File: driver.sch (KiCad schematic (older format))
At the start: 45 parts, among them J1 Screw_Terminal_01x02, J2 Conn_02x12_Odd_Even, Q10 Q_NMOS_GDSD, Q11 Q_NMOS_GDSD, Q12 Q_NMOS_GDSD, Q13 Q_NMOS_GDSD, Q14 Q_NMOS_GDSD, Q15 Q_NMOS_GDSD, Q16 Q_NMOS_GDSD, Q17 IRF9Z34 PMOS_DGS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

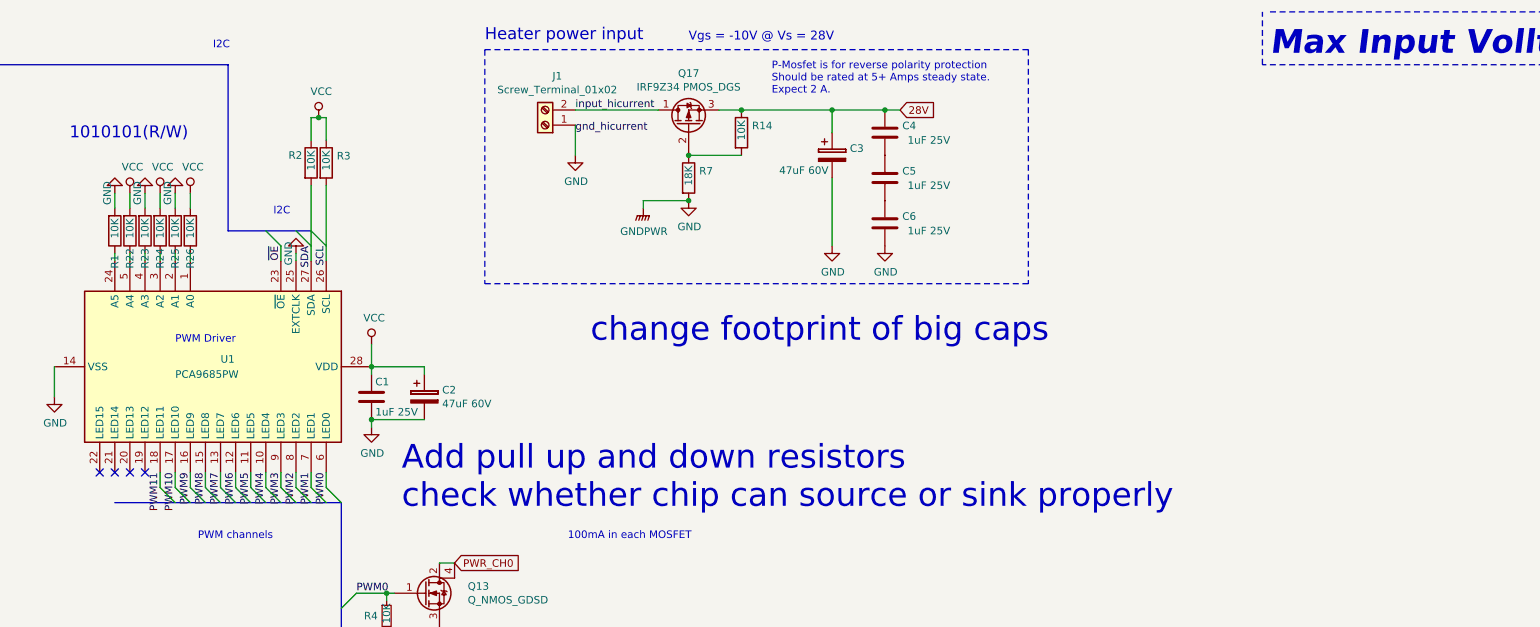
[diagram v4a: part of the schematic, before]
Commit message: resistor value/footprint changes and associated routing changes
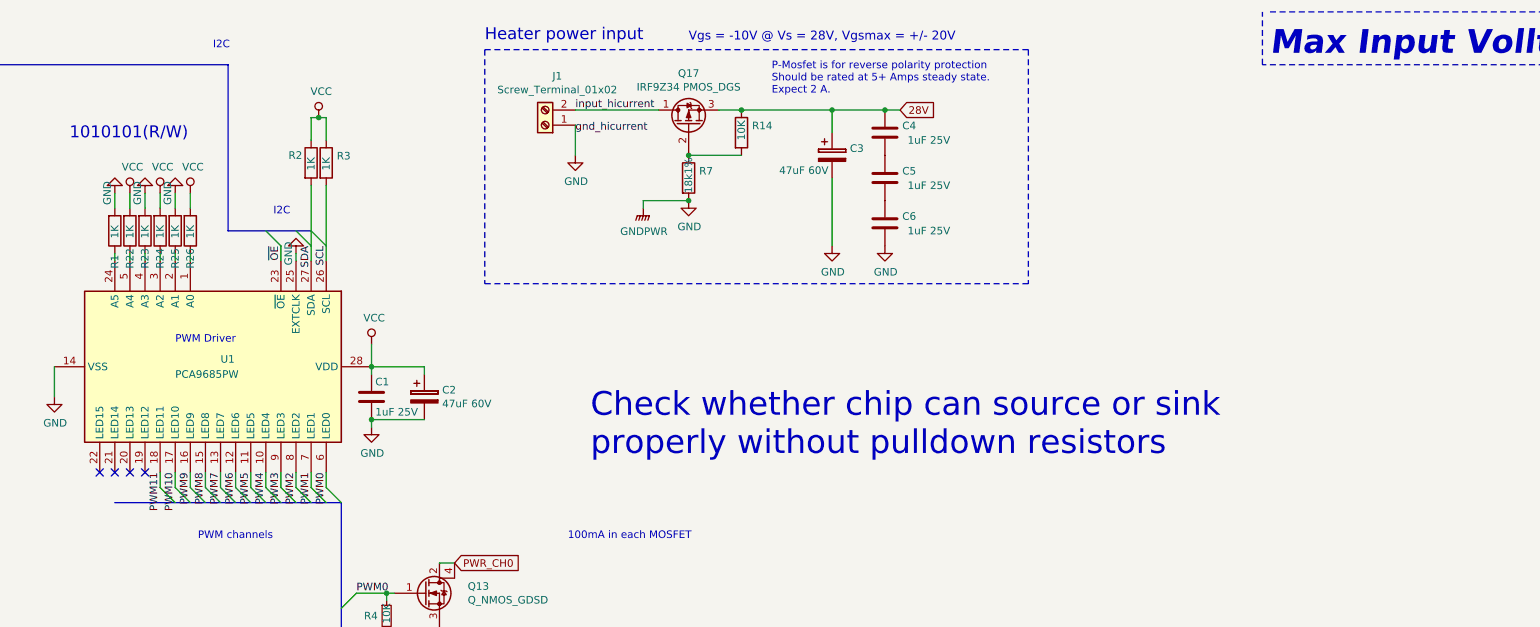
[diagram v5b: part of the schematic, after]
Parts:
- R1, R2, R22, R23, R24, R25, R26, R3: value 10K -> 1K
- R10, R11, R12, R13, R14, R18, R19, R20, R21, R4, R5, R6, R9: footprint Resistor_SMD:R_0805_2012Metric_Pad1.15x1.40mm_HandSolder -> Resistor_SMD:R_1206_3216Metric_Pad1.42x1.75mm_HandSolder
- R7: value 18K -> 18k1%; footprint Resistor_SMD:R_0805_2012Metric_Pad1.15x1.40mm_HandSolder -> Resistor_SMD:R_1206_3216Metric_Pad1.42x1.75mm_HandSolder
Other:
- note added: "Check whether chip can source or sink \nproperly without pulldown resistors"
- note added: "Vgs = -10V @ Vs = 28V, Vgsmax = +/- 20V"
- note removed: "Add pull up and down resistors\ncheck whether chip can source or sink properly"
- note removed: "Vgs = -10V @ Vs = 28V"
- note removed: "change footprint of big caps"
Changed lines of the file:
@@
 P 5100 2150
 F 0 "R1" V 5100 2400 50  0000 R CNN
-F 1 "10K" V 5100 2200 50  0000 R CNN
+F 1 "1K" V 5100 2200 50  0000 R CNN
 F 2 "Resistor_SMD:R_0805_2012Metric_Pad1.15x1.40mm_HandSolder" V 5030 2150 50  0001 C CNN
 F 3 "~" H 5100 2150 50  0001 C CNN
@@
 P 8900 1800
 F 0 "R7" H 8970 1846 50  0000 L CNN
-F 1 "18K" V 8900 1750 50  0000 L CNN
-F 2 "Resistor_SMD:R_0805_2012Metric_Pad1.15x1.40mm_HandSolder" V 8830 1800 50  0001 C CNN
+F 1 "18k1%" V 8900 1700 50  0000 L CNN
+F 2 "Resistor_SMD:R_1206_3216Metric_Pad1.42x1.75mm_HandSolder" V 8830 1800 50  0001 C CNN
 F 3 "~" H 8900 1800 50  0001 C CNN
 	1    8900 1800
@@
 P 6500 1700
 F 0 "R3" H 6570 1746 50  0000 L CNN
-F 1 "10K" V 6500 1650 50  0000 L CNN
+F 1 "1K" V 6500 1650 50  0000 L CNN
 F 2 "Resistor_SMD:R_0805_2012Metric_Pad1.15x1.40mm_HandSolder" V 6430 1700 50  0001 C CNN
 F 3 "~" H 6500 1700 50  0001 C CNN
@@
 P 6400 1700
 F 0 "R2" H 6250 1750 50  0000 L CNN
-F 1 "10K" V 6400 1650 50  0000 L CNN
+F 1 "1K" V 6400 1650 50  0000 L CNN
 F 2 "Resistor_SMD:R_0805_2012Metric_Pad1.15x1.40mm_HandSolder" V 6330 1700 50  0001 C CNN
 F 3 "~" H 6400 1700 50  0001 C CNN
@@
 	6500 1400 6500 1550
 Connection ~ 6450 1400
-Text Notes 7000 4000 0    157  ~ 0
-Add pull up and down resistors\ncheck whether chip can source or sink properly
-Text Notes 8250 2900 0    157  ~ 0
-change footprint of big caps
+Text Notes 8250 3650 0    157  ~ 0
+Check whether chip can source or sink \nproperly without pulldown resistors
 $Comp
 L Device:R_Small R4
@@
 F 0 "R4" H 6750 4700 50  0000 L CNN
 F 1 "10K" V 6900 4650 50  0000 L CNN
-F 2 "Resistor_SMD:R_0805_2012Metric_Pad1.15x1.40mm_HandSolder" H 6900 4700 50  0001 C CNN
+F 2 "Resistor_SMD:R_1206_3216Metric_Pad1.42x1.75mm_HandSolder" H 6900 4700 50  0001 C CNN
 F 3 "~" H 6900 4700 50  0001 C CNN
 	1    6900 4700
@@
 F 0 "R5" H 6750 5300 50  0000 L CNN
 F 1 "10K" V 6900 5250 50  0000 L CNN
-F 2 "Resistor_SMD:R_0805_2012Metric_Pad1.15x1.40mm_HandSolder" H 6900 5300 50  0001 C CNN
+F 2 "Resistor_SMD:R_1206_3216Metric_Pad1.42x1.75mm_HandSolder" H 6900 5300 50  0001 C CNN
 F 3 "~" H 6900 5300 50  0001 C CNN
 	1    6900 5300
@@
 F 0 "R6" H 6750 5900 50  0000 L CNN
 F 1 "10K" V 6900 5850 50  0000 L CNN
-F 2 "Resistor_SMD:R_0805_2012Metric_Pad1.15x1.40mm_HandSolder" H 6900 5900 50  0001 C CNN
+F 2 "Resistor_SMD:R_1206_3216Metric_Pad1.42x1.75mm_HandSolder" H 6900 5900 50  0001 C CNN
 F 3 "~" H 6900 5900 50  0001 C CNN
 	1    6900 5900
@@
 F 0 "R9" H 6750 6500 50  0000 L CNN
 F 1 "10K" V 6900 6450 50  0000 L CNN
-F 2 "Resistor_SMD:R_0805_2012Metric_Pad1.15x1.40mm_HandSolder" H 6900 6500 50  0001 C CNN
+F 2 "Resistor_SMD:R_1206_3216Metric_Pad1.42x1.75mm_HandSolder" H 6900 6500 50  0001 C CNN
 F 3 "~" H 6900 6500 50  0001 C CNN
 	1    6900 6500
@@
 F 0 "R10" H 6700 7100 50  0000 L CNN
 F 1 "10K" V 6900 7050 50  0000 L CNN
-F 2 "Resistor_SMD:R_0805_2012Metric_Pad1.15x1.40mm_HandSolder" H 6900 7100 50  0001 C CNN
+F 2 "Resistor_SMD:R_1206_3216Metric_Pad1.42x1.75mm_HandSolder" H 6900 7100 50  0001 C CNN
 F 3 "~" H 6900 7100 50  0001 C CNN
 	1    6900 7100
@@
 F 0 "R11" H 6700 7700 50  0000 L CNN
 F 1 "10K" V 6900 7650 50  0000 L CNN
-F 2 "Resistor_SMD:R_0805_2012Metric_Pad1.15x1.40mm_HandSolder" H 6900 7700 50  0001 C CNN
+F 2 "Resistor_SMD:R_1206_3216Metric_Pad1.42x1.75mm_HandSolder" H 6900 7700 50  0001 C CNN
 F 3 "~" H 6900 7700 50  0001 C CNN
 	1    6900 7700
@@
 F 0 "R12" H 6700 8300 50  0000 L CNN
 F 1 "10K" V 6900 8250 50  0000 L CNN
-F 2 "Resistor_SMD:R_0805_2012Metric_Pad1.15x1.40mm_HandSolder" H 6900 8300 50  0001 C CNN
+F 2 "Resistor_SMD:R_1206_3216Metric_Pad1.42x1.75mm_HandSolder" H 6900 8300 50  0001 C CNN
 F 3 "~" H 6900 8300 50  0001 C CNN
 	1    6900 8300
@@
 F 0 "R13" H 6700 8900 50  0000 L CNN
 F 1 "10K" V 6900 8850 50  0000 L CNN
-F 2 "Resistor_SMD:R_0805_2012Metric_Pad1.15x1.40mm_HandSolder" H 6900 8900 50  0001 C CNN
+F 2 "Resistor_SMD:R_1206_3216Metric_Pad1.42x1.75mm_HandSolder" H 6900 8900 50  0001 C CNN
 F 3 "~" H 6900 8900 50  0001 C CNN
 	1    6900 8900
@@
 F 0 "R21" H 8150 8900 50  0000 L CNN
 F 1 "10K" V 8350 8850 50  0000 L CNN
-F 2 "Resistor_SMD:R_0805_2012Metric_Pad1.15x1.40mm_HandSolder" H 8350 8900 50  0001 C CNN
+F 2 "Resistor_SMD:R_1206_3216Metric_Pad1.42x1.75mm_HandSolder" H 8350 8900 50  0001 C CNN
 F 3 "~" H 8350 8900 50  0001 C CNN
 	1    8350 8900
@@
 F 0 "R20" H 8100 8300 50  0000 L CNN
 F 1 "10K" V 8300 8250 50  0000 L CNN
-F 2 "Resistor_SMD:R_0805_2012Metric_Pad1.15x1.40mm_HandSolder" H 8300 8300 50  0001 C CNN
+F 2 "Resistor_SMD:R_1206_3216Metric_Pad1.42x1.75mm_HandSolder" H 8300 8300 50  0001 C CNN
 F 3 "~" H 8300 8300 50  0001 C CNN
 	1    8300 8300
@@
 F 0 "R19" H 8100 7700 50  0000 L CNN
 F 1 "10K" V 8300 7650 50  0000 L CNN
-F 2 "Resistor_SMD:R_0805_2012Metric_Pad1.15x1.40mm_HandSolder" H 8300 7700 50  0001 C CNN
+F 2 "Resistor_SMD:R_1206_3216Metric_Pad1.42x1.75mm_HandSolder" H 8300 7700 50  0001 C CNN
 F 3 "~" H 8300 7700 50  0001 C CNN
 	1    8300 7700
@@
 F 0 "R18" H 8100 7100 50  0000 L CNN
 F 1 "10K" V 8300 7050 50  0000 L CNN
-F 2 "Resistor_SMD:R_0805_2012Metric_Pad1.15x1.40mm_HandSolder" H 8300 7100 50  0001 C CNN
+F 2 "Resistor_SMD:R_1206_3216Metric_Pad1.42x1.75mm_HandSolder" H 8300 7100 50  0001 C CNN
 F 3 "~" H 8300 7100 50  0001 C CNN
 	1    8300 7100
@@
 P 5300 2150
 F 0 "R23" V 5300 2400 50  0000 R CNN
-F 1 "10K" V 5300 2200 50  0000 R CNN
+F 1 "1K" V 5300 2200 50  0000 R CNN
 F 2 "Resistor_SMD:R_0805_2012Metric_Pad1.15x1.40mm_HandSolder" V 5230 2150 50  0001 C CNN
 F 3 "~" H 5300 2150 50  0001 C CNN
@@
 P 5400 2150
 F 0 "R24" V 5400 2400 50  0000 R CNN
-F 1 "10K" V 5400 2200 50  0000 R CNN
+F 1 "1K" V 5400 2200 50  0000 R CNN
 F 2 "Resistor_SMD:R_0805_2012Metric_Pad1.15x1.40mm_HandSolder" V 5330 2150 50  0001 C CNN
 F 3 "~" H 5400 2150 50  0001 C CNN
@@
 P 5200 2150
 F 0 "R22" V 5200 2400 50  0000 R CNN
-F 1 "10K" V 5200 2200 50  0000 R CNN
+F 1 "1K" V 5200 2200 50  0000 R CNN
 F 2 "Resistor_SMD:R_0805_2012Metric_Pad1.15x1.40mm_HandSolder" V 5130 2150 50  0001 C CNN
 F 3 "~" H 5200 2150 50  0001 C CNN
@@
 P 5500 2150
 F 0 "R25" V 5500 2400 50  0000 R CNN
-F 1 "10K" V 5500 2200 50  0000 R CNN
+F 1 "1K" V 5500 2200 50  0000 R CNN
 F 2 "Resistor_SMD:R_0805_2012Metric_Pad1.15x1.40mm_HandSolder" V 5430 2150 50  0001 C CNN
 F 3 "~" H 5500 2150 50  0001 C CNN
@@
 P 5600 2150
 F 0 "R26" V 5600 2400 50  0000 R CNN
-F 1 "10K" V 5600 2200 50  0000 R CNN
+F 1 "1K" V 5600 2200 50  0000 R CNN
 F 2 "Resistor_SMD:R_0805_2012Metric_Pad1.15x1.40mm_HandSolder" V 5530 2150 50  0001 C CNN
 F 3 "~" H 5600 2150 50  0001 C CNN
@@
 F 0 "R14" H 9320 1546 50  0000 L CNN
 F 1 "10K" V 9250 1450 50  0000 L CNN
-F 2 "Resistor_SMD:R_0805_2012Metric_Pad1.15x1.40mm_HandSolder" V 9180 1500 50  0001 C CNN
+F 2 "Resistor_SMD:R_1206_3216Metric_Pad1.42x1.75mm_HandSolder" V 9180 1500 50  0001 C CNN
 F 3 "~" H 9250 1500 50  0001 C CNN
 	1    9250 1500
@@
 	8650 7750 8650 7800
 Text Notes 8900 900  0    59   ~ 0
-Vgs = -10V @ Vs = 28V
-Wire Wire Line
-	6500 1850 6500 2350
+Vgs = -10V @ Vs = 28V, Vgsmax = +/- 20V
 Wire Wire Line
 	9850 1800 9850 2250
@@
 NoConn ~ 2050 2150
 Wire Wire Line
+	6500 1850 6500 2350
+Wire Bus Line
+	5850 2150 6400 2150
+Wire Wire Line
 	6400 1850 6400 2350
 Wire Bus Line
-	5850 2150 6400 2150
-Wire Bus Line
 	8050 7050 8050 9400

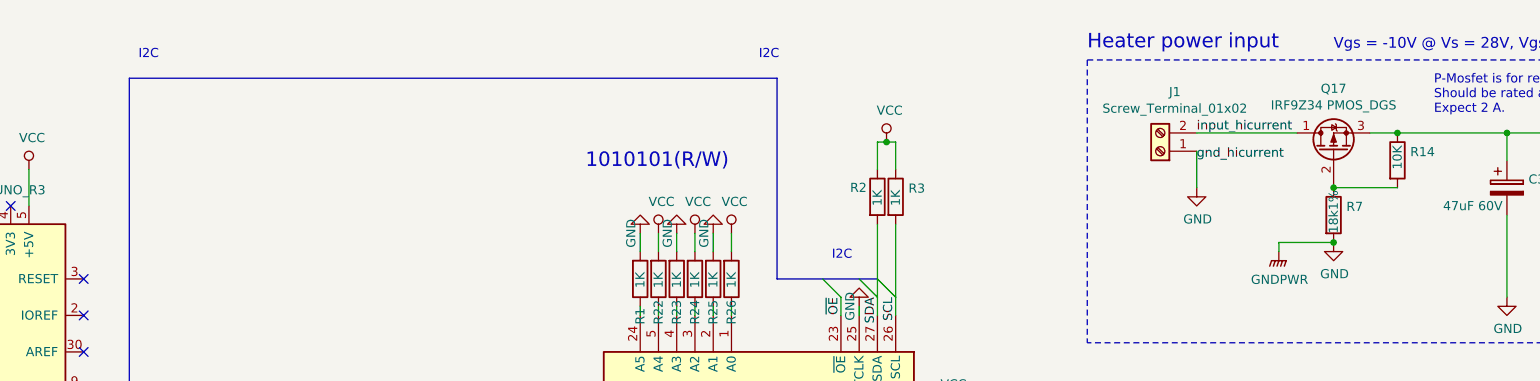
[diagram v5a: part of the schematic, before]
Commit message: update for mosfet pinout change
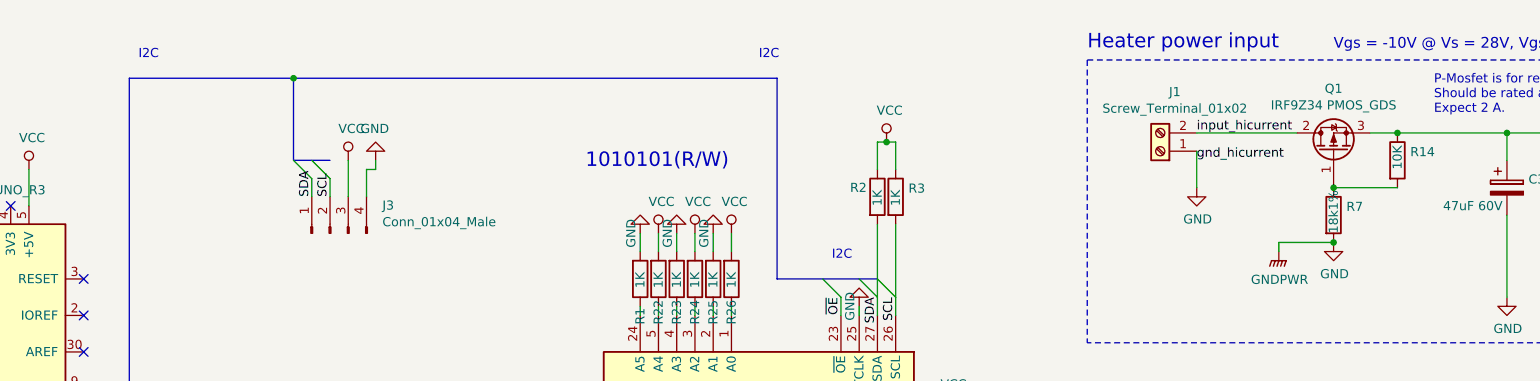
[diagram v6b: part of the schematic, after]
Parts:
- removed Q17: IRF9Z34 PMOS_DGS, Package_TO_SOT_THT:TO-220-3_Vertical, symbol Device:Q_PMOS_DGS
- added J3: Conn_01x04_Male, Connector_PinHeader_1.27mm:PinHeader_1x04_P1.27mm_Vertical, symbol Connector:Conn_01x04_Male
- added Q1: IRF9Z34 PMOS_GDS, Package_TO_SOT_THT:TO-220-3_Vertical, symbol Device:Q_PMOS_GDS
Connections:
- net 28V: now also Q1.3 (S)
- net GND: now also J3.4 (Pin_4)
- net SCL: now also J3.2 (Pin_2)
- net SDA: now also J3.1 (Pin_1)
- net VCC: now also J3.3 (Pin_3)
- net input_hicurrent: now also Q1.2 (D)
- net at R14.2, R7.1: now also Q1.1 (G)
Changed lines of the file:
@@
 $EndComp
 Wire Bus Line
-	5850 1050 2300 1050
+	5850 1050 3200 1050
 Entry Wire Line
 	6400 2150 6500 2250
@@
 	-1   0    0    1
 $EndComp
-$Comp
-L Device:Q_PMOS_DGS Q17
-U 1 1 5C429FD6
-P 8900 1450
-F 0 "Q17" V 9243 1450 50  0000 C CNN
-F 1 "IRF9Z34 PMOS_DGS" V 9152 1450 50  0000 C CNN
-F 2 "Package_TO_SOT_THT:TO-220-3_Vertical" H 9100 1550 50  0001 C CNN
-F 3 "~" H 8900 1450 50  0001 C CNN
-	1    8900 1450
-	0    -1   -1   0
-$EndComp
 Wire Wire Line
 	8150 1350 8700 1350
@@
 Wire Wire Line
 	9250 1650 8900 1650
-Connection ~ 8900 1650
 $Comp
 L power:GND #PWR020
@@
 	7550 950  7550 2500
 NoConn ~ 2050 2150
+$Comp
+L Connector:Conn_01x04_Male J3
+U 1 1 5C54F291
+P 3400 1900
+F 0 "J3" V 3553 1613 50  0000 R CNN
+F 1 "Conn_01x04_Male" V 3462 1613 50  0000 R CNN
+F 2 "Connector_PinHeader_1.27mm:PinHeader_1x04_P1.27mm_Vertical" H 3400 1900 50  0001 C CNN
+F 3 "~" H 3400 1900 50  0001 C CNN
+	1    3400 1900
+	0    -1   -1   0
+$EndComp
+Wire Bus Line
+	3200 1500 3200 1050
+Connection ~ 3200 1050
+Wire Bus Line
+	3200 1050 2300 1050
+Entry Wire Line
+	3200 1500 3300 1600
+Entry Wire Line
+	3300 1500 3400 1600
+Wire Wire Line
+	3300 1600 3300 1700
+Wire Wire Line
+	3400 1600 3400 1700
+Text Label 3300 1700 1    50   ~ 0
+SDA
+Text Label 3400 1700 1    50   ~ 0
+SCL
+$Comp
+L power:VCC #PWR02
+U 1 1 5C55CB70
+P 3500 1500
+F 0 "#PWR02" H 3500 1350 50  0001 C CNN
+F 1 "VCC" H 3517 1673 50  0000 C CNN
+F 2 "" H 3500 1500 50  0001 C CNN
+F 3 "" H 3500 1500 50  0001 C CNN
+	1    3500 1500
+	1    0    0    -1
+$EndComp
+Wire Wire Line
+	3500 1500 3500 1700
+$Comp
+L power:GND #PWR03
+U 1 1 5C5616C7
+P 3650 1500
+F 0 "#PWR03" H 3650 1250 50  0001 C CNN
+F 1 "GND" H 3655 1327 50  0000 C CNN
+F 2 "" H 3650 1500 50  0001 C CNN
+F 3 "" H 3650 1500 50  0001 C CNN
+	1    3650 1500
+	-1   0    0    1
+$EndComp
+Wire Wire Line
+	3650 1500 3650 1550
+Wire Wire Line
+	3650 1550 3600 1550
+Wire Wire Line
+	3600 1550 3600 1700
 Wire Wire Line
 	6500 1850 6500 2350
+Wire Bus Line
+	3200 1500 3400 1500
 Wire Bus Line
 	5850 2150 6400 2150
@@
 Wire Bus Line
 	5100 3950 6600 3950
+$Comp
+L Device:Q_PMOS_GDS Q1
+U 1 1 5C5B9973
+P 8900 1450
+F 0 "Q1" V 9243 1450 50  0000 C CNN
+F 1 "IRF9Z34 PMOS_GDS" V 9152 1450 50  0000 C CNN
+F 2 "Package_TO_SOT_THT:TO-220-3_Vertical" H 9100 1550 50  0001 C CNN
+F 3 "~" H 8900 1450 50  0001 C CNN
+	1    8900 1450
+	0    -1   -1   0
+$EndComp
+Connection ~ 8900 1650
 $EndSCHEMATC

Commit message: final version, sending to GA
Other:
- note added: "GA / Team OTheRS\nJacob Killelea"
- note added: "Heater Driver"
- note removed: "Heater Driver PCB"
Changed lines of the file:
@@
 Text Notes 10100 5200 0    50   ~ 0
 Connector to heaters is just a pin header.\nRated at 1 A per contact
-Text Notes 11900 10300 0    157  ~ 0
-Heater Driver PCB
+Text Notes 11900 10500 0    157  ~ 31
+GA / Team OTheRS\nJacob Killelea
 $Comp
 L Device:CP C3
@@
 Wire Wire Line
 	3600 1550 3600 1700
+$Comp
+L Device:Q_PMOS_GDS Q1
+U 1 1 5C5B9973
+P 8900 1450
+F 0 "Q1" V 9243 1450 50  0000 C CNN
+F 1 "IRF9Z34 PMOS_GDS" V 9152 1450 50  0000 C CNN
+F 2 "Package_TO_SOT_THT:TO-220-3_Vertical" H 9100 1550 50  0001 C CNN
+F 3 "~" H 8900 1450 50  0001 C CNN
+	1    8900 1450
+	0    -1   -1   0
+$EndComp
+Connection ~ 8900 1650
 Wire Wire Line
 	6500 1850 6500 2350
@@
 Wire Bus Line
 	5100 3950 6600 3950
-$Comp
-L Device:Q_PMOS_GDS Q1
-U 1 1 5C5B9973
-P 8900 1450
-F 0 "Q1" V 9243 1450 50  0000 C CNN
-F 1 "IRF9Z34 PMOS_GDS" V 9152 1450 50  0000 C CNN
-F 2 "Package_TO_SOT_THT:TO-220-3_Vertical" H 9100 1550 50  0001 C CNN
-F 3 "~" H 8900 1450 50  0001 C CNN
-	1    8900 1450
-	0    -1   -1   0
-$EndComp
-Connection ~ 8900 1650
+Text Notes 12300 10950 0    118  ~ 0
+Heater Driver
 $EndSCHEMATC
